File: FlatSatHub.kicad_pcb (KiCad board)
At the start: 4 copper layers, 166.3 x 166.3 mm, 39 parts, among them J1 Jack-DC, J10 DB26_Male_HighDensity_Mountin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, J11 Conn_02x02_Odd_Even, J12 DB26_Male_HighDensity_Mountin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, J13 Conn_02x02_Odd_Even, J14 DB26_Male_HighDensity_Mountin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, J15 Conn_02x02_Odd_Even, J16 DB26_Male_HighDensity_Mountin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, J17 Conn_02x02_Odd_Even, J2 DB26_Male_HighDensity_Mountin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

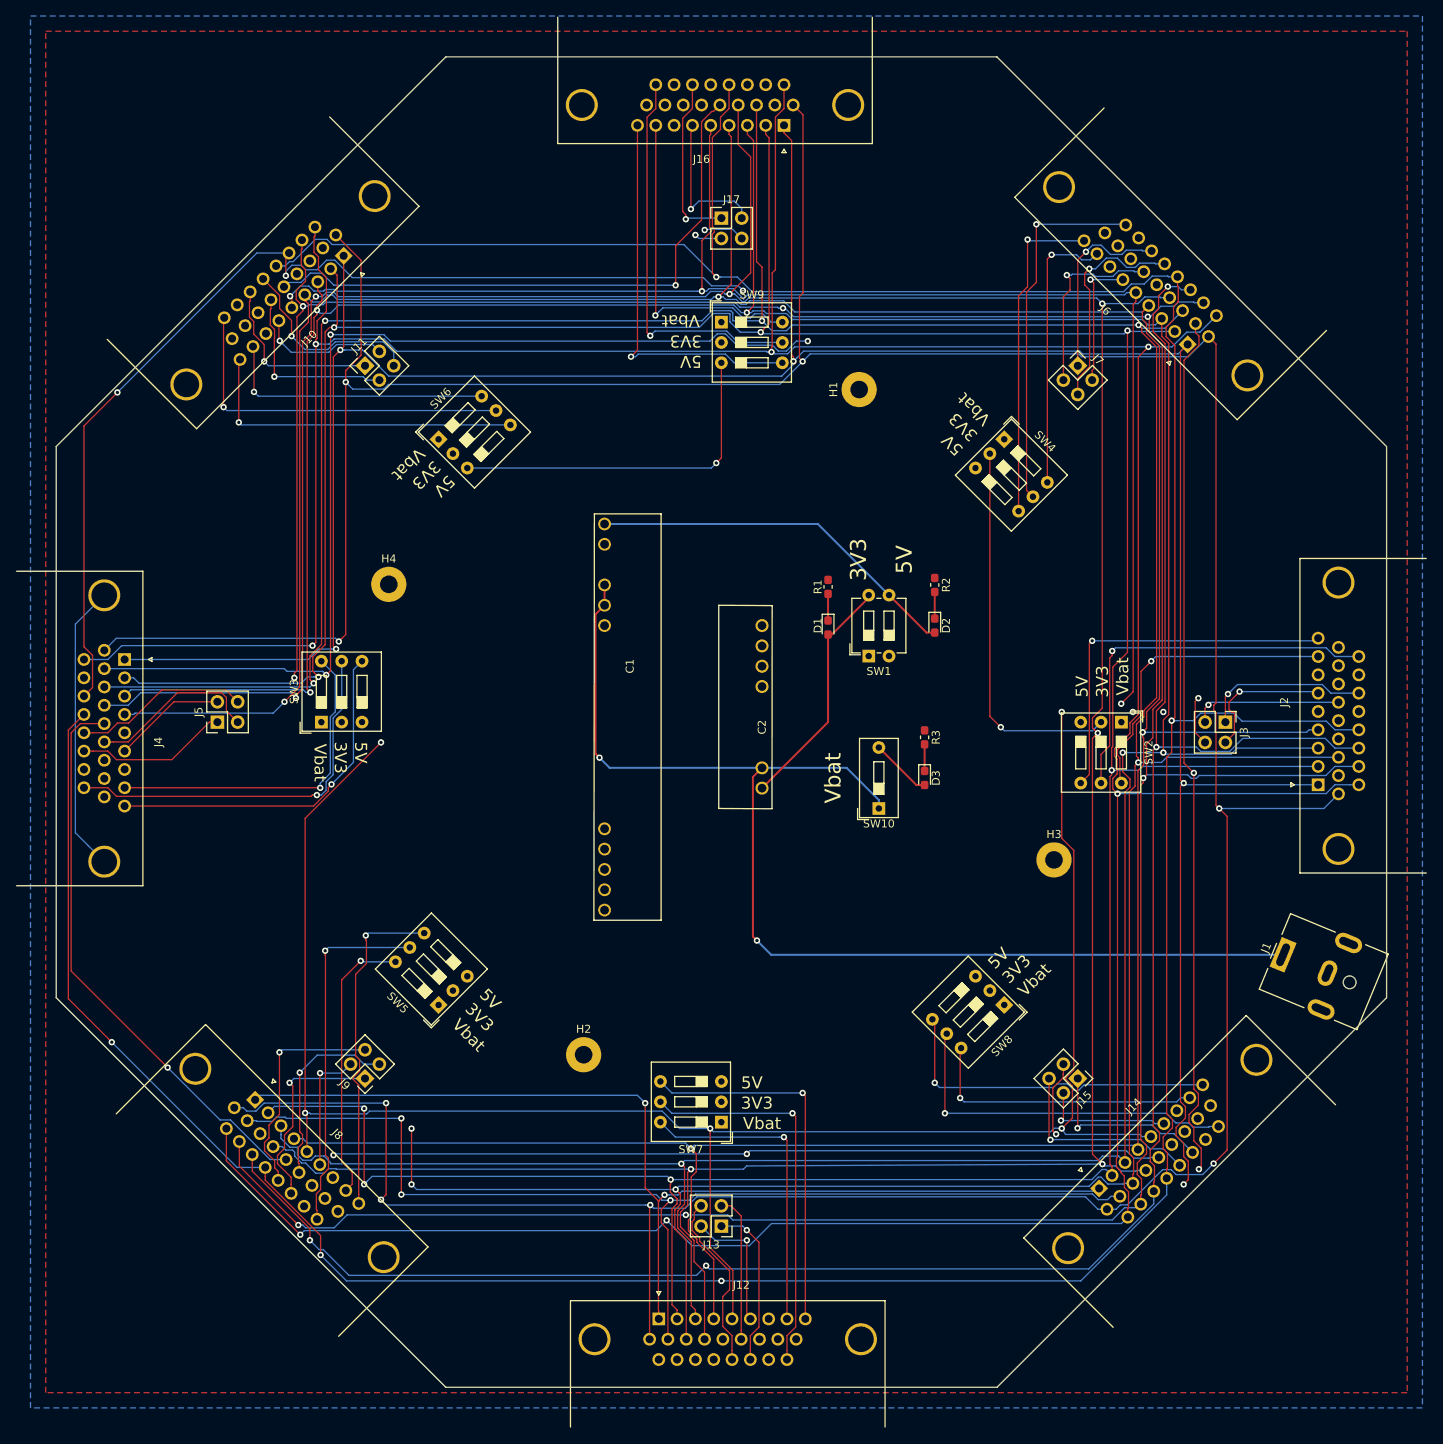
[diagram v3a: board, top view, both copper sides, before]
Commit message: new UART layout and rewire
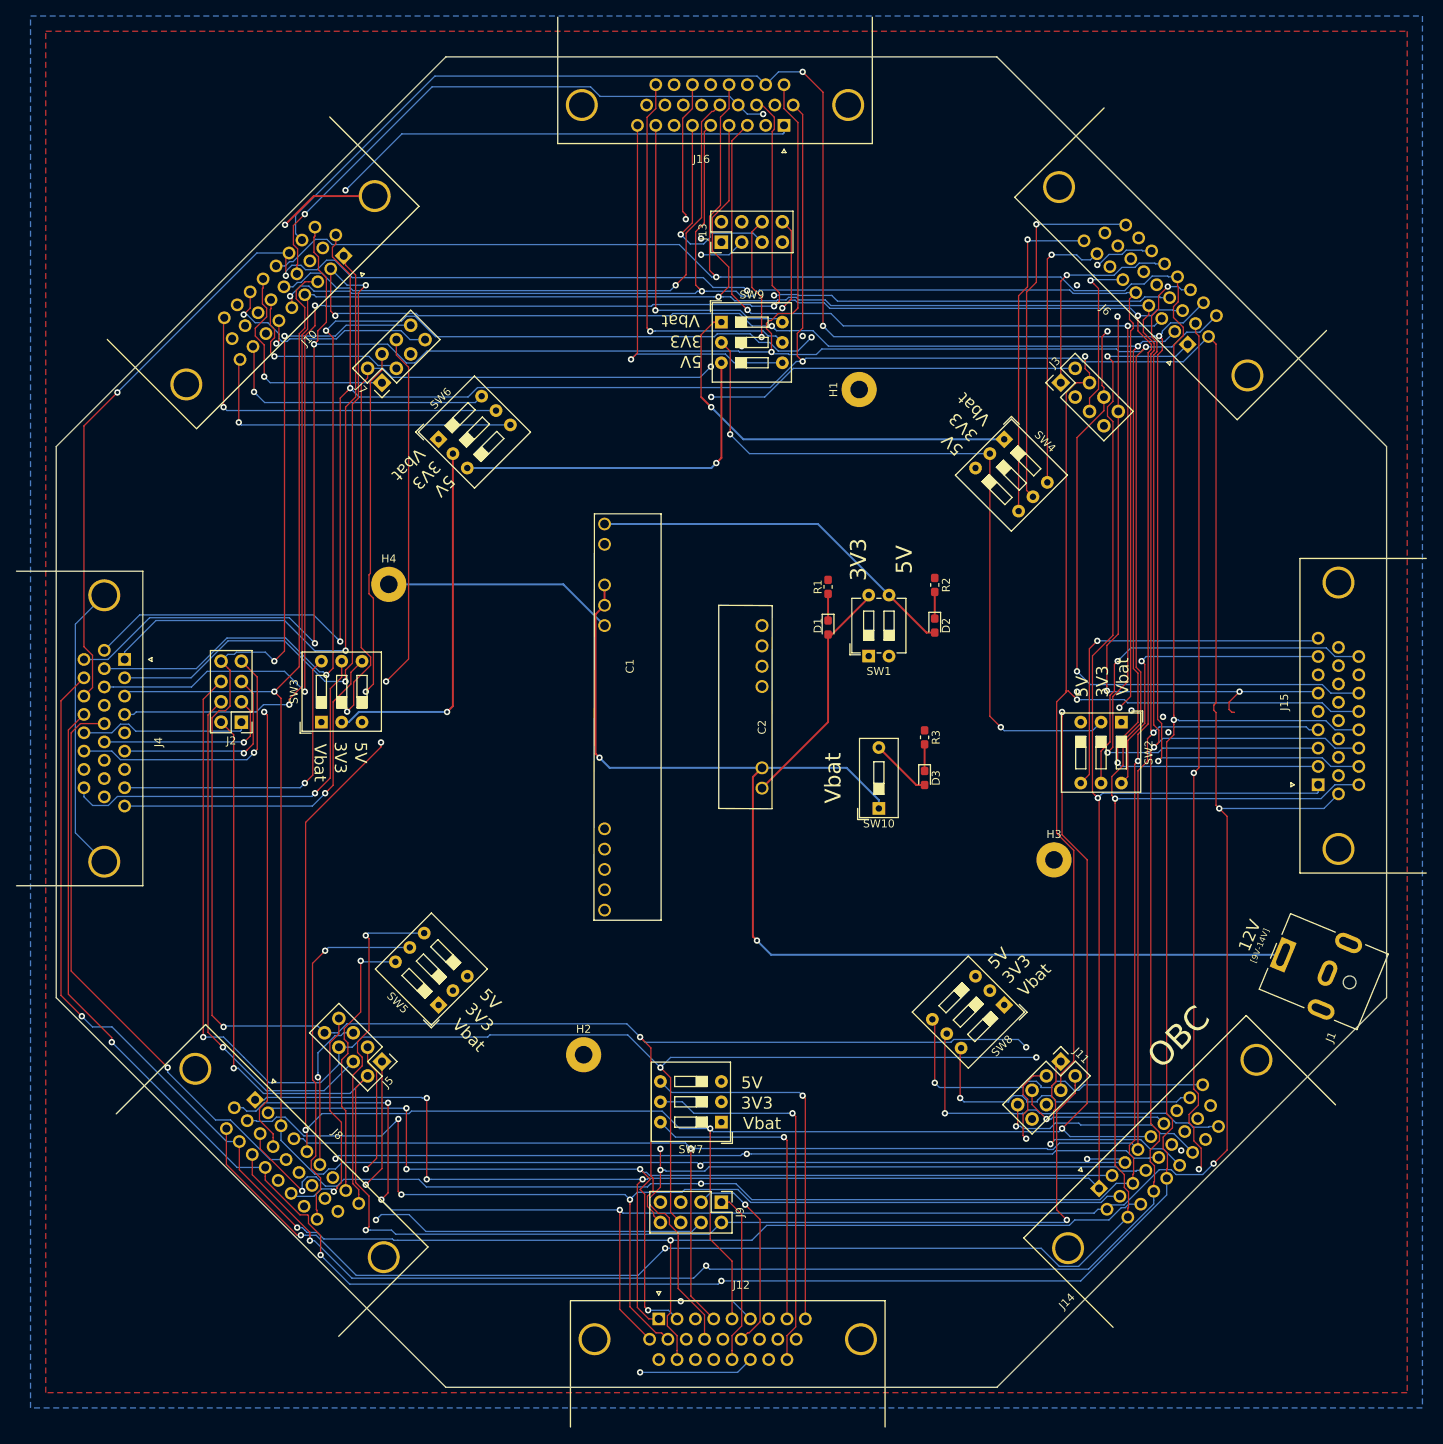
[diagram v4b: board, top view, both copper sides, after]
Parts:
- removed J17: Conn_02x02_Odd_Even, Connector_PinHeader_2.54mm:PinHeader_2x02_P2.54mm_Vertical
- J11, J13, J3, J5, J7, J9: value Conn_02x02_Odd_Even -> HEADER_4x2; footprint Connector_PinHeader_2.54mm:PinHeader_2x02_P2.54mm_Vertical -> Connector_PinHeader_2.54mm:PinHeader_2x04_P2.54mm_Vertical
- J15: value Conn_02x02_Odd_Even -> DB26_Male_HighDensity_MountingHoles; footprint Connector_PinHeader_2.54mm:PinHeader_2x02_P2.54mm_Vertical -> DB-HD-26:DSUB-26-HD_Male_Horizontal_P2.29x1.98mm_EdgePinOffset8.35mm_Housed_MountingHolesOffset10.89mm
- J2: value DB26_Male_HighDensity_MountingHoles -> HEADER_4x2; footprint DB-HD-26:DSUB-26-HD_Male_Horizontal_P2.29x1.98mm_EdgePinOffset8.35mm_Housed_MountingHolesOffset10.89mm -> Connector_PinHeader_2.54mm:PinHeader_2x04_P2.54mm_Vertical
- moved J2 134.8 mm to (34.8, 101.7), turned to 180 degrees
- moved J13 123.0 mm to (94.8, 41.6), turned to 90 degrees
- moved J11 123.0 mm to (137.2, 144.1), turned to 315 degrees
- moved J7 87.0 mm to (52.3, 59.2), turned to 135 degrees
- moved J15 47.4 mm to (169.3, 109.5), turned to 90 degrees
- moved J9 47.2 mm to (94.8, 161.7), turned to 270 degrees
- moved J3 47.2 mm to (137.2, 59.2), turned to 45 degrees
- moved J5 47.2 mm to (52.3, 144.1), turned to 225 degrees
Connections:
- J11 pad 1: /sheet5F23178F/UART2_TX -> /sheet5F237BCE/UART1_RX
- J11 pad 2: /sheet5F23178F/UART2_RX -> OBC_UART1_TX
- J11 pad 3: /sheet5F23178F/UART1_TX -> /sheet5F237BCE/UART1_TX
- J11 pad 4: /sheet5F23178F/UART1_RX -> OBC_UART1_RX
- J13 pad 1: /sheet5F231790/UART2_TX -> /sheet5F237BCF/UART1_RX
- J13 pad 2: /sheet5F231790/UART2_RX -> OBC_UART1_TX
- J13 pad 3: /sheet5F231790/UART1_TX -> /sheet5F237BCF/UART1_TX
- J13 pad 4: /sheet5F231790/UART1_RX -> OBC_UART1_RX
- J15 pad 1: /sheet5F237BCE/UART2_TX -> /I2C2_SDA
- J15 pad 2: /sheet5F237BCE/UART2_RX -> /SPI1_MISO
- J15 pad 3: /sheet5F237BCE/UART1_TX -> /SPI1_SS
- J15 pad 4: /sheet5F237BCE/UART1_RX -> /SPI4_SS
- J2 pad 1: /I2C2_SDA -> /sheet5F22A1B0/UART1_RX
- J2 pad 2: /SPI1_MISO -> OBC_UART1_TX
- J2 pad 3: /SPI1_SS -> /sheet5F22A1B0/UART1_TX
- J2 pad 4: /SPI4_SS -> OBC_UART1_RX
- J2 pad 5: /CAN1_TX -> /sheet5F22A1B0/UART2_RX
- J2 pad 6: /sheet5F1F8E85/UART2_RX -> OBC_UART2_TX
- J2 pad 7: Net-(J2-Pad7) -> /sheet5F22A1B0/UART2_TX
- J2 pad 8: /sheet5F1F8E85/bus_vbat -> OBC_UART2_RX
- J3 pad 1: /sheet5F1F8E85/UART2_TX -> /sheet5F22D1E8/UART1_RX
- J3 pad 2: /sheet5F1F8E85/UART2_RX -> OBC_UART1_TX
- J3 pad 3: /sheet5F1F8E85/UART1_TX -> /sheet5F22D1E8/UART1_TX
- J3 pad 4: /sheet5F1F8E85/UART1_RX -> OBC_UART1_RX
- J5 pad 1: /sheet5F22A1B0/UART2_TX -> /sheet5F22D1E9/UART1_RX
- J5 pad 2: /sheet5F22A1B0/UART2_RX -> OBC_UART1_TX
- J5 pad 3: /sheet5F22A1B0/UART1_TX -> /sheet5F22D1E9/UART1_TX
- J5 pad 4: /sheet5F22A1B0/UART1_RX -> OBC_UART1_RX
- J7 pad 1: /sheet5F22D1E8/UART2_TX -> /sheet5F23178F/UART1_RX
- J7 pad 2: /sheet5F22D1E8/UART2_RX -> OBC_UART1_TX
- J7 pad 3: /sheet5F22D1E8/UART1_TX -> /sheet5F23178F/UART1_TX
- J7 pad 4: /sheet5F22D1E8/UART1_RX -> OBC_UART1_RX
- J9 pad 1: /sheet5F22D1E9/UART2_TX -> /sheet5F231790/UART1_RX
- J9 pad 2: /sheet5F22D1E9/UART2_RX -> OBC_UART1_TX
- J9 pad 3: /sheet5F22D1E9/UART1_TX -> /sheet5F231790/UART1_TX
- J9 pad 4: /sheet5F22D1E9/UART1_RX -> OBC_UART1_RX
- SW2 pad 4: /sheet5F1F8E85/bus_5v -> /Sheet5F2C117D/bus_5v
- SW2 pad 5: /sheet5F1F8E85/bus_3v3 -> /Sheet5F2C117D/bus_3v3
- SW2 pad 6: /sheet5F1F8E85/bus_vbat -> /Sheet5F2C117D/bus_vbat
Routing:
- net OBC_UART1_TX: track 0.00 -> 441.9 mm, vias 0 -> 7
- net OBC_UART2_TX: track 0.00 -> 438.0 mm, vias 0 -> 7
- net OBC_UART1_RX: track 0.00 -> 430.7 mm, vias 0 -> 6
- net OBC_UART2_RX: track 0.00 -> 430.0 mm, vias 0 -> 9
- net 3V3: track 47.9 -> 139.6 mm, vias 1 -> 3
- net Vbat: track 7.66 -> 58.7 mm, vias 0 -> 1
- net /sheet5F1F8E85/bus_3v3: track 48.5 -> 0.00 mm, vias 1 -> 0
- net /Sheet5F2C117D/bus_3v3: track 0.00 -> 47.4 mm, vias 0 -> 1
- net /sheet5F1F8E85/bus_5v: track 46.8 -> 0.00 mm, vias 1 -> 0
- net /Sheet5F2C117D/bus_5v: track 0.00 -> 46.4 mm, vias 0 -> 1
- net GND: track 52.5 -> 94.3 mm, vias 0 -> 1
- net /Sheet5F2C117D/bus_vbat: track 0.00 -> 39.2 mm, vias 0 -> 1
- net /sheet5F1F8E85/bus_vbat: track 38.3 -> 0.00 mm, vias 1 -> 0
- net /sheet5F1F8E85/UART1_RX: track 27.0 -> 0.00 mm, vias 1 -> 0
- net /sheet5F1F8E85/UART2_TX: track 20.9 -> 0.00 mm, vias 1 -> 0
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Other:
- board text added: "12V"
- board text added: "OBC"
- board text added: "[9V-14V]"

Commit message: add silkscreen for uarts
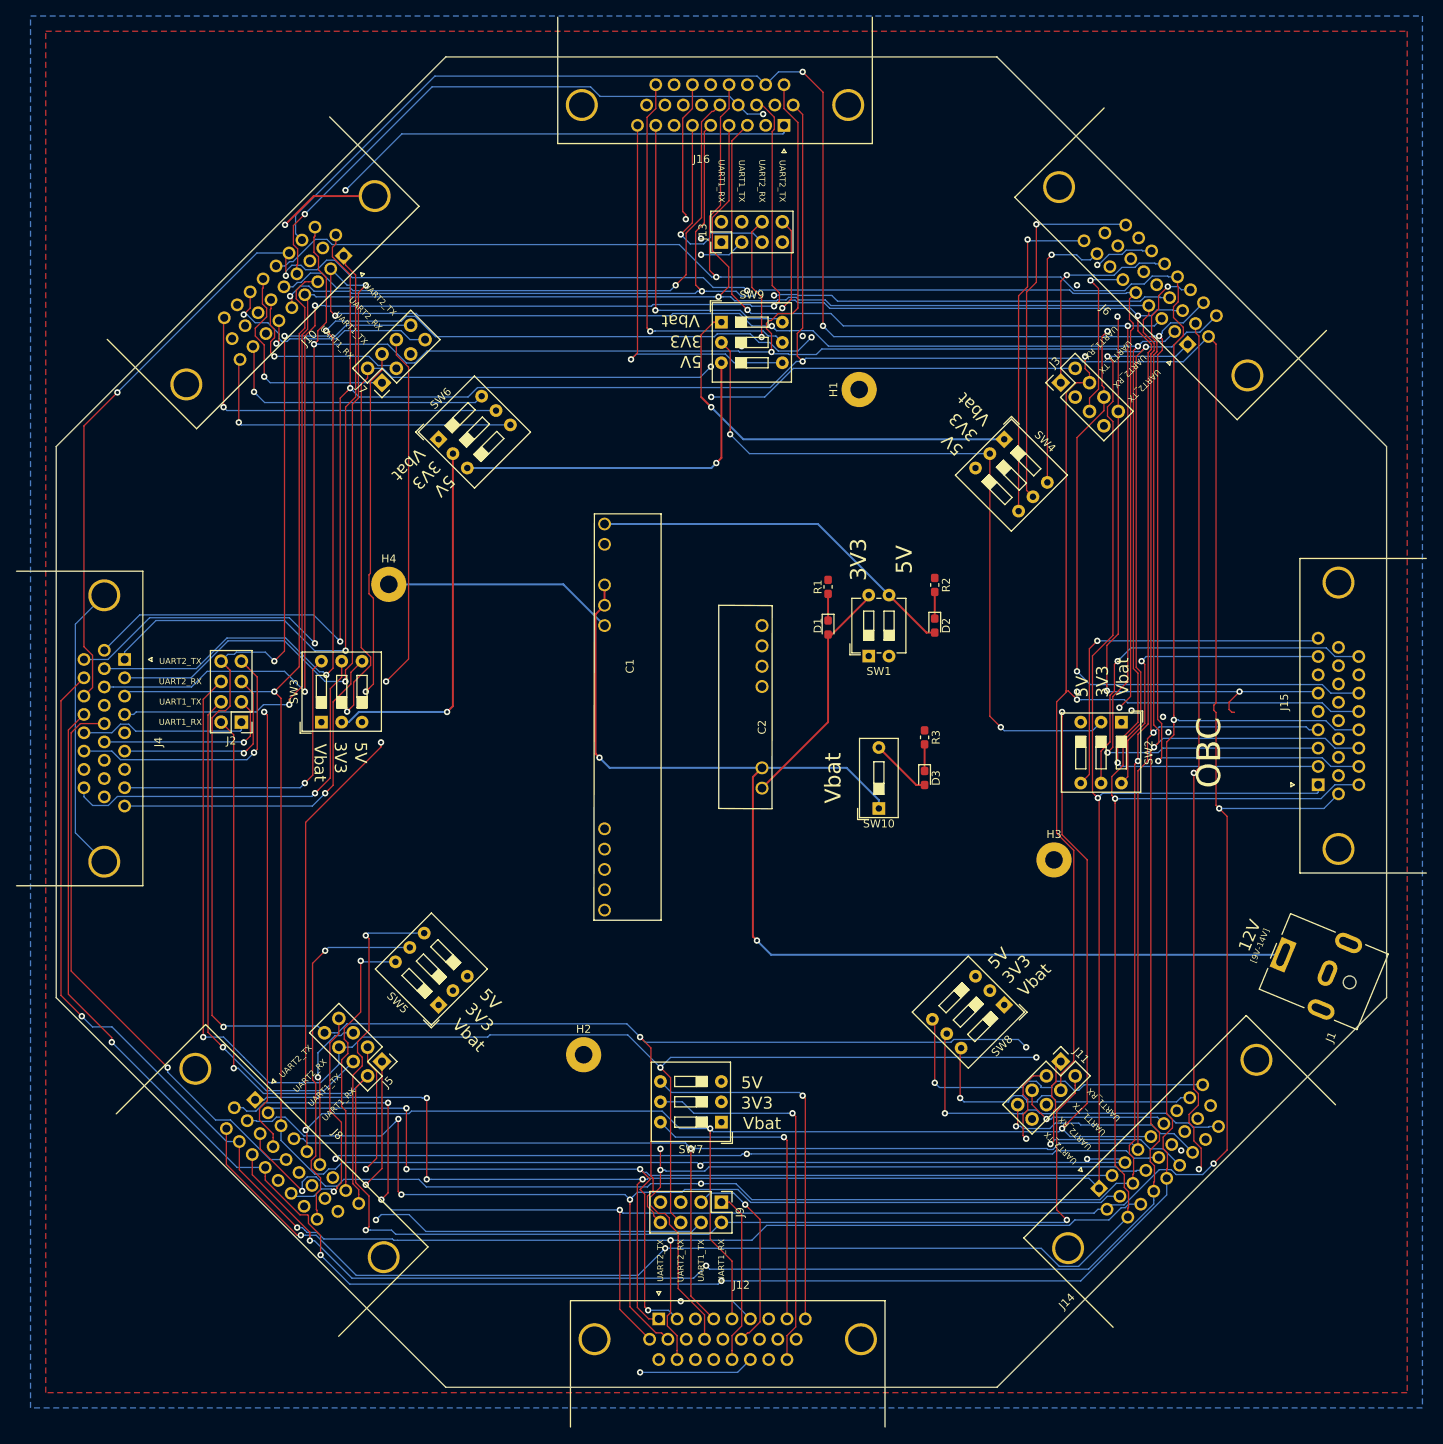
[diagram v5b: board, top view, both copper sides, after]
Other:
- board text added: "UART1_RX"
- board text added: "UART1_TX"
- board text added: "UART2_RX"
- board text added: "UART2_TX"
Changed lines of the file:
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@@
   (general
     (thickness 1.6)
-    (drawings 38)
+    (drawings 66)
     (tracks 2084)
     (zones 0)
@@
   )
   (setup
-    (last_trace_width 0.15)
+    (last_trace_width 0.25)
     (user_trace_width 0.15)
     (user_trace_width 0.25)
@@
       (net 5 "Net-(C2-Pad4)"))
   )
+  (gr_text "UART1_RX\n" (at 46.925489 149.442989 45) (layer F.SilkS)
+    (effects (font (size 0.75 0.75) (thickness 0.1)))
+  )
+  (gr_text "UART1_TX\n" (at 45.129438 147.646938 45) (layer F.SilkS)
+    (effects (font (size 0.75 0.75) (thickness 0.1)))
+  )
+  (gr_text "UART2_TX\n" (at 41.537336 144.054836 45) (layer F.SilkS)
+    (effects (font (size 0.75 0.75) (thickness 0.1)))
+  )
+  (gr_text "UART2_RX\n" (at 43.333387 145.850887 45) (layer F.SilkS)
+    (effects (font (size 0.75 0.75) (thickness 0.1)))
+  )
+  (gr_text "UART1_RX\n" (at 27.12 101.65) (layer F.SilkS)
+    (effects (font (size 0.75 0.75) (thickness 0.1)))
+  )
+  (gr_text "UART1_TX\n" (at 27.12 99.11) (layer F.SilkS)
+    (effects (font (size 0.75 0.75) (thickness 0.1)))
+  )
+  (gr_text "UART2_TX\n" (at 27.12 94.03) (layer F.SilkS)
+    (effects (font (size 0.75 0.75) (thickness 0.1)))
+  )
+  (gr_text "UART2_RX\n" (at 27.12 96.57) (layer F.SilkS)
+    (effects (font (size 0.75 0.75) (thickness 0.1)))
+  )
+  (gr_text "UART1_RX\n" (at 46.684511 54.192989 315) (layer F.SilkS)
+    (effects (font (size 0.75 0.75) (thickness 0.1)))
+  )
+  (gr_text "UART1_TX\n" (at 48.480562 52.396938 315) (layer F.SilkS)
+    (effects (font (size 0.75 0.75) (thickness 0.1)))
+  )
+  (gr_text "UART2_TX\n" (at 52.072664 48.804836 315) (layer F.SilkS)
+    (effects (font (size 0.75 0.75) (thickness 0.1)))
+  )
+  (gr_text "UART2_RX\n" (at 50.276613 50.600887 315) (layer F.SilkS)
+    (effects (font (size 0.75 0.75) (thickness 0.1)))
+  )
+  (gr_text "UART1_RX\n" (at 94.755 34.015 270) (layer F.SilkS)
+    (effects (font (size 0.75 0.75) (thickness 0.1)))
+  )
+  (gr_text "UART1_TX\n" (at 97.295 34.015 270) (layer F.SilkS)
+    (effects (font (size 0.75 0.75) (thickness 0.1)))
+  )
+  (gr_text "UART2_TX\n" (at 102.375 34.015 270) (layer F.SilkS)
+    (effects (font (size 0.75 0.75) (thickness 0.1)))
+  )
+  (gr_text "UART2_RX\n" (at 99.835 34.015 270) (layer F.SilkS)
+    (effects (font (size 0.75 0.75) (thickness 0.1)))
+  )
+  (gr_text "UART1_RX\n" (at 142.212011 54.214511 225) (layer F.SilkS)
+    (effects (font (size 0.75 0.75) (thickness 0.1)))
+  )
+  (gr_text "UART1_TX\n" (at 144.008062 56.010562 225) (layer F.SilkS)
+    (effects (font (size 0.75 0.75) (thickness 0.1)))
+  )
+  (gr_text "UART2_TX\n" (at 147.600164 59.602664 225) (layer F.SilkS)
+    (effects (font (size 0.75 0.75) (thickness 0.1)))
+  )
+  (gr_text "UART2_RX\n" (at 145.804113 57.806613 225) (layer F.SilkS)
+    (effects (font (size 0.75 0.75) (thickness 0.1)))
+  )
+  (gr_text "UART1_RX\n" (at 142.547989 149.479511 135) (layer F.SilkS)
+    (effects (font (size 0.75 0.75) (thickness 0.1)))
+  )
+  (gr_text "UART1_TX\n" (at 140.751938 151.275562 135) (layer F.SilkS)
+    (effects (font (size 0.75 0.75) (thickness 0.1)))
+  )
+  (gr_text "UART2_TX\n" (at 137.159836 154.867664 135) (layer F.SilkS)
+    (effects (font (size 0.75 0.75) (thickness 0.1)))
+  )
+  (gr_text "UART2_RX\n" (at 138.955887 153.071613 135) (layer F.SilkS)
+    (effects (font (size 0.75 0.75) (thickness 0.1)))
+  )
+  (gr_text "UART1_RX\n" (at 94.755 168.96 90) (layer F.SilkS)
+    (effects (font (size 0.75 0.75) (thickness 0.1)))
+  )
+  (gr_text "UART1_TX\n" (at 92.215 168.96 90) (layer F.SilkS)
+    (effects (font (size 0.75 0.75) (thickness 0.1)))
+  )
+  (gr_text "UART2_RX\n" (at 89.675 168.96 90) (layer F.SilkS)
+    (effects (font (size 0.75 0.75) (thickness 0.1)))
+  )
+  (gr_text "UART2_TX\n" (at 87.135 168.96 90) (layer F.SilkS)
+    (effects (font (size 0.75 0.75) (thickness 0.1)))
+  )
   (gr_text 12V (at 160.795 128.32 67.5) (layer F.SilkS)
     (effects (font (size 1.5 1.5) (thickness 0.3)))
@@
     (effects (font (size 0.75 0.75) (thickness 0.1875)))
   )
-  (gr_text OBC (at 151.905 141.02 45) (layer F.SilkS)
+  (gr_text OBC (at 155.715 105.46 90) (layer F.SilkS)
     (effects (font (size 3 3) (thickness 0.5)))
   )
